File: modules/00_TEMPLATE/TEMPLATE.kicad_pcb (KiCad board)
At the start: 2 copper layers, 160 x 100 mm, 2 parts, among them J1 Card_Connector

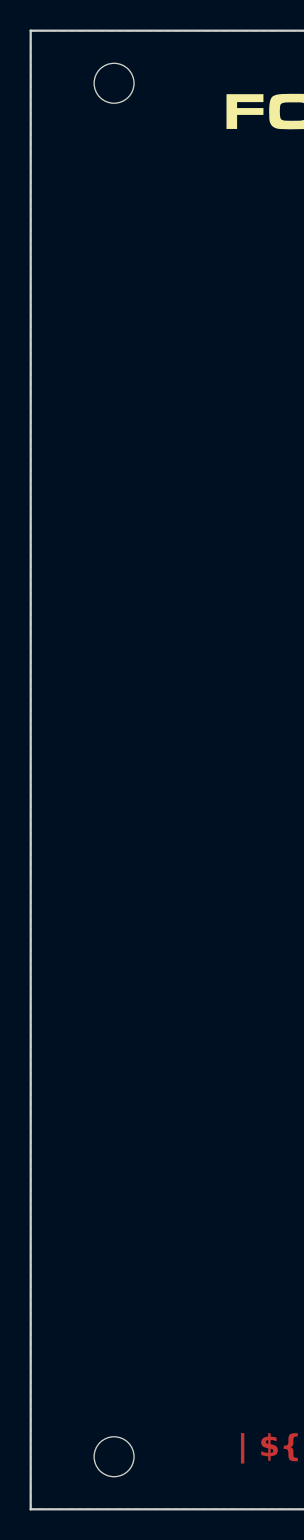
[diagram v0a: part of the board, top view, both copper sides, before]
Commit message: fixed card bracket footprint
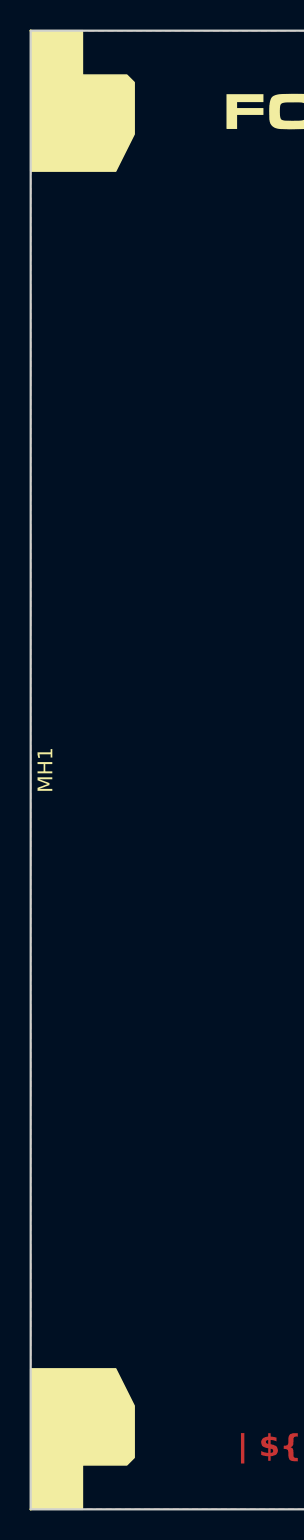
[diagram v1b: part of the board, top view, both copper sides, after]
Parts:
- MH1: value ~ -> CardBracket; footprint FormantKO:Schroff_60807-011_3U_Pair -> FormantKO:Card_Bracket
- moved MH1 50.0 mm to (55.0, 95.0)

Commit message: panel updates & vco
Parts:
- moved J1 40.2 mm to (215.0, 95.0)
